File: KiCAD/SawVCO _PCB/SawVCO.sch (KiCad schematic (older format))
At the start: 46 parts, among them J1 PWR_IN, J10 Saw_Out, J2 Liner_FM, J3 PWR_OUT, J4 I_Ref, J5 I_Sink, J6 TP_GND, J7 Sync_In, J8 Saw_Out, J9 Saw_Out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

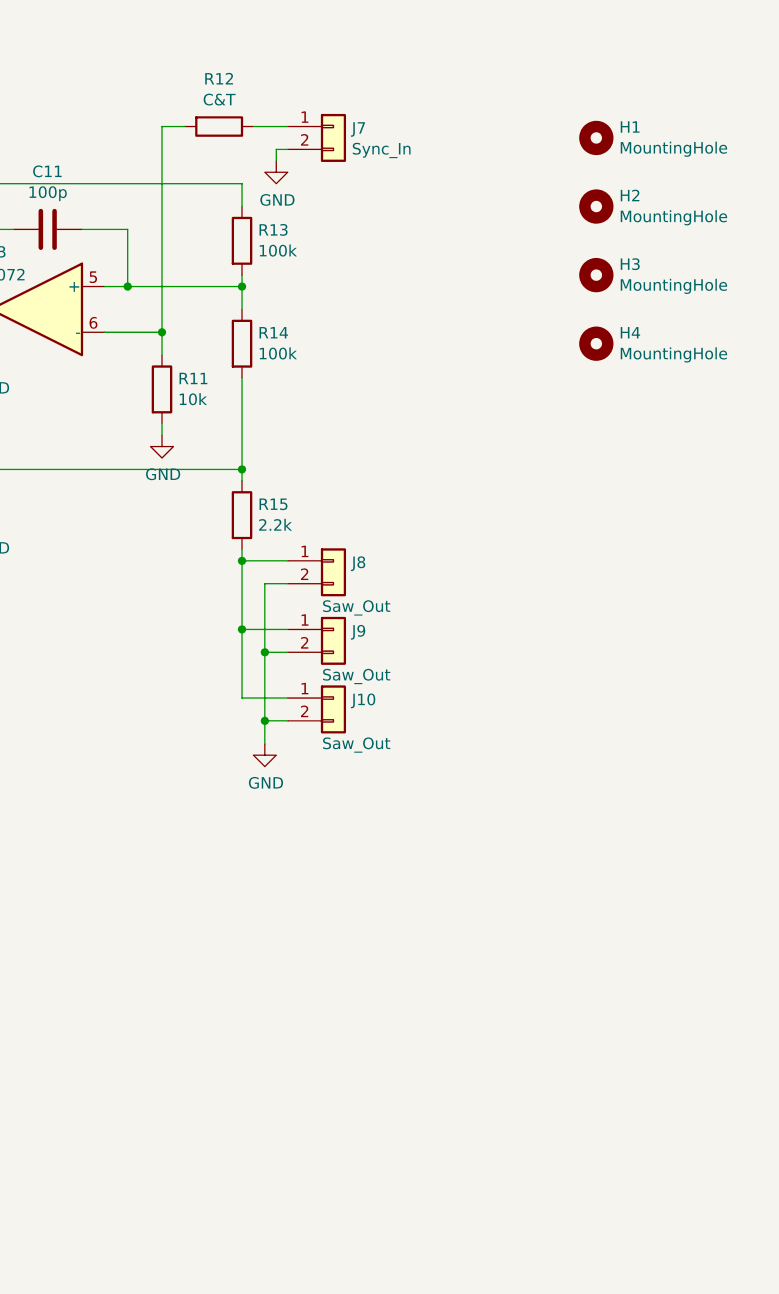
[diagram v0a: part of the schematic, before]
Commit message: Add +5V Output
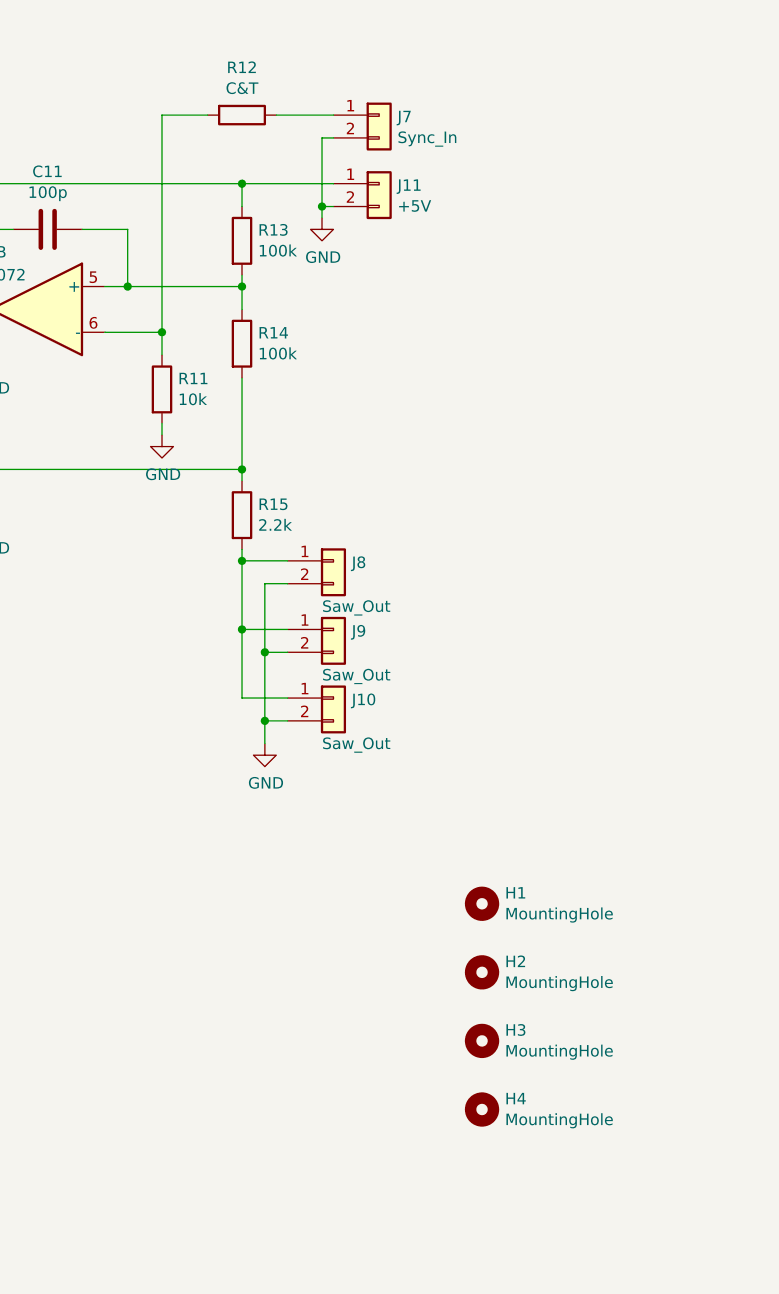
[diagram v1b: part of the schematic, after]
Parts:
- added J11: +5V, Connector_JST:JST_XH_B2B-XH-A_1x02_P2.50mm_Vertical, symbol Connector_Generic:Conn_01x02
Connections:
- net +5V: now also J11.1 (Pin_1)
- net GND: now also J11.2 (Pin_2)
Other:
- moved on the sheet: H1, H2, H3, H4, J7, R12
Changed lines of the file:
@@
 Sheet 1 1
 Title "SawVCO"
-Date "2020-10-18"
+Date "2020-10-19"
 Rev "Ver. 1.0"
 Comp "PNPN Manufactory"
@@
 L Device:R R12
 U 1 1 5F866B82
-P 7800 1500
-F 0 "R12" V 7593 1500 50  0000 C CNN
-F 1 "C&T" V 7684 1500 50  0000 C CNN
-F 2 "Resistor_THT:R_Axial_DIN0207_L6.3mm_D2.5mm_P7.62mm_Horizontal" V 7730 1500 50  0001 C CNN
-F 3 "~" H 7800 1500 50  0001 C CNN
-	1    7800 1500
+P 7900 1450
+F 0 "R12" V 7693 1450 50  0000 C CNN
+F 1 "C&T" V 7784 1450 50  0000 C CNN
+F 2 "Resistor_THT:R_Axial_DIN0207_L6.3mm_D2.5mm_P7.62mm_Horizontal" V 7830 1450 50  0001 C CNN
+F 3 "~" H 7900 1450 50  0001 C CNN
+	1    7900 1450
 	0    1    1    0
 $EndComp
 Wire Wire Line
-	7550 2400 7550 1500
-Wire Wire Line
-	7550 1500 7650 1500
+	7550 2400 7550 1450
+Wire Wire Line
+	7550 1450 7750 1450
 Connection ~ 7550 2400
 $Comp
 L Connector_Generic:Conn_01x02 J7
 U 1 1 5F86A584
-P 8300 1500
-F 0 "J7" H 8380 1492 50  0000 L CNN
-F 1 "Sync_In" H 8380 1401 50  0000 L CNN
-F 2 "Connector_JST:JST_XH_B2B-XH-A_1x02_P2.50mm_Vertical" H 8300 1500 50  0001 C CNN
-F 3 "~" H 8300 1500 50  0001 C CNN
-	1    8300 1500
-	1    0    0    -1
-$EndComp
-Wire Wire Line
-	7950 1500 8100 1500
-$Comp
-L power:GND #PWR025
-U 1 1 5F86CF11
-P 8050 1650
-F 0 "#PWR025" H 8050 1400 50  0001 C CNN
-F 1 "GND" H 8055 1477 50  0000 C CNN
-F 2 "" H 8050 1650 50  0001 C CNN
-F 3 "" H 8050 1650 50  0001 C CNN
-	1    8050 1650
-	1    0    0    -1
-$EndComp
-Wire Wire Line
-	8100 1600 8050 1600
-Wire Wire Line
-	8050 1600 8050 1650
+P 8500 1450
+F 0 "J7" H 8580 1442 50  0000 L CNN
+F 1 "Sync_In" H 8580 1351 50  0000 L CNN
+F 2 "Connector_JST:JST_XH_B2B-XH-A_1x02_P2.50mm_Vertical" H 8500 1450 50  0001 C CNN
+F 3 "~" H 8500 1450 50  0001 C CNN
+	1    8500 1450
+	1    0    0    -1
+$EndComp
+Wire Wire Line
+	8050 1450 8300 1450
 $Comp
 L Connector_Generic:Conn_01x02 J8
@@
 L Mechanical:MountingHole H1
 U 1 1 5F95CBBF
-P 9450 1550
-F 0 "H1" H 9550 1596 50  0000 L CNN
-F 1 "MountingHole" H 9550 1505 50  0000 L CNN
-F 2 "MountingHole:MountingHole_3.2mm_M3" H 9450 1550 50  0001 C CNN
-F 3 "~" H 9450 1550 50  0001 C CNN
-	1    9450 1550
+P 8950 4900
+F 0 "H1" H 9050 4946 50  0000 L CNN
+F 1 "MountingHole" H 9050 4855 50  0000 L CNN
+F 2 "MountingHole:MountingHole_3.2mm_M3" H 8950 4900 50  0001 C CNN
+F 3 "~" H 8950 4900 50  0001 C CNN
+	1    8950 4900
 	1    0    0    -1
 $EndComp
@@
 L Mechanical:MountingHole H2
 U 1 1 5F95D449
-P 9450 1850
-F 0 "H2" H 9550 1896 50  0000 L CNN
-F 1 "MountingHole" H 9550 1805 50  0000 L CNN
-F 2 "MountingHole:MountingHole_3.2mm_M3" H 9450 1850 50  0001 C CNN
-F 3 "~" H 9450 1850 50  0001 C CNN
-	1    9450 1850
+P 8950 5200
+F 0 "H2" H 9050 5246 50  0000 L CNN
+F 1 "MountingHole" H 9050 5155 50  0000 L CNN
+F 2 "MountingHole:MountingHole_3.2mm_M3" H 8950 5200 50  0001 C CNN
+F 3 "~" H 8950 5200 50  0001 C CNN
+	1    8950 5200
 	1    0    0    -1
 $EndComp
@@
 L Mechanical:MountingHole H3
 U 1 1 5F95E277
-P 9450 2150
-F 0 "H3" H 9550 2196 50  0000 L CNN
-F 1 "MountingHole" H 9550 2105 50  0000 L CNN
-F 2 "MountingHole:MountingHole_3.2mm_M3" H 9450 2150 50  0001 C CNN
-F 3 "~" H 9450 2150 50  0001 C CNN
-	1    9450 2150
+P 8950 5500
+F 0 "H3" H 9050 5546 50  0000 L CNN
+F 1 "MountingHole" H 9050 5455 50  0000 L CNN
+F 2 "MountingHole:MountingHole_3.2mm_M3" H 8950 5500 50  0001 C CNN
+F 3 "~" H 8950 5500 50  0001 C CNN
+	1    8950 5500
 	1    0    0    -1
 $EndComp
@@
 L Mechanical:MountingHole H4
 U 1 1 5F95F134
-P 9450 2450
-F 0 "H4" H 9550 2496 50  0000 L CNN
-F 1 "MountingHole" H 9550 2405 50  0000 L CNN
-F 2 "MountingHole:MountingHole_3.2mm_M3" H 9450 2450 50  0001 C CNN
-F 3 "~" H 9450 2450 50  0001 C CNN
-	1    9450 2450
-	1    0    0    -1
-$EndComp
+P 8950 5800
+F 0 "H4" H 9050 5846 50  0000 L CNN
+F 1 "MountingHole" H 9050 5755 50  0000 L CNN
+F 2 "MountingHole:MountingHole_3.2mm_M3" H 8950 5800 50  0001 C CNN
+F 3 "~" H 8950 5800 50  0001 C CNN
+	1    8950 5800
+	1    0    0    -1
+$EndComp
+$Comp
+L Connector_Generic:Conn_01x02 J11
+U 1 1 5F8F836B
+P 8500 1750
+F 0 "J11" H 8580 1742 50  0000 L CNN
+F 1 "+5V" H 8580 1651 50  0000 L CNN
+F 2 "Connector_JST:JST_XH_B2B-XH-A_1x02_P2.50mm_Vertical" H 8500 1750 50  0001 C CNN
+F 3 "~" H 8500 1750 50  0001 C CNN
+	1    8500 1750
+	1    0    0    -1
+$EndComp
+$Comp
+L power:GND #PWR025
+U 1 1 5F8F8D03
+P 8250 1900
+F 0 "#PWR025" H 8250 1650 50  0001 C CNN
+F 1 "GND" H 8255 1727 50  0000 C CNN
+F 2 "" H 8250 1900 50  0001 C CNN
+F 3 "" H 8250 1900 50  0001 C CNN
+	1    8250 1900
+	1    0    0    -1
+$EndComp
+Wire Wire Line
+	8300 1750 7900 1750
+Connection ~ 7900 1750
+Wire Wire Line
+	8300 1850 8250 1850
+Wire Wire Line
+	8250 1850 8250 1900
+Wire Wire Line
+	8300 1550 8250 1550
+Wire Wire Line
+	8250 1550 8250 1850
+Connection ~ 8250 1850
 $EndSCHEMATC

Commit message: 結合テスト
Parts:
- RV1: value 10k -> 5k; footprint Potentiometer_THT:Potentiometer_Bourns_3296W_Vertical -> Potentiometer_THT:Potentiometer_Bourns_3296X_Horizontal
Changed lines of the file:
@@
 Sheet 1 1
 Title "SawVCO"
-Date "2020-10-19"
+Date "2020-10-21"
 Rev "Ver. 1.0"
 Comp "PNPN Manufactory"
@@
 P 5000 2900
 F 0 "RV1" H 4930 2946 50  0000 R CNN
-F 1 "10k" H 4930 2855 50  0000 R CNN
-F 2 "Potentiometer_THT:Potentiometer_Bourns_3296W_Vertical" H 5000 2900 50  0001 C CNN
+F 1 "5k" H 4930 2855 50  0000 R CNN
+F 2 "Potentiometer_THT:Potentiometer_Bourns_3296X_Horizontal" H 5000 2900 50  0001 C CNN
 F 3 "~" H 5000 2900 50  0001 C CNN
 	1    5000 2900
